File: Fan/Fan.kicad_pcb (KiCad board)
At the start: 2 copper layers, 32.5 x 14.5 mm, 25 parts, among them Q1 Hum Sensor, U2 HEF4093B

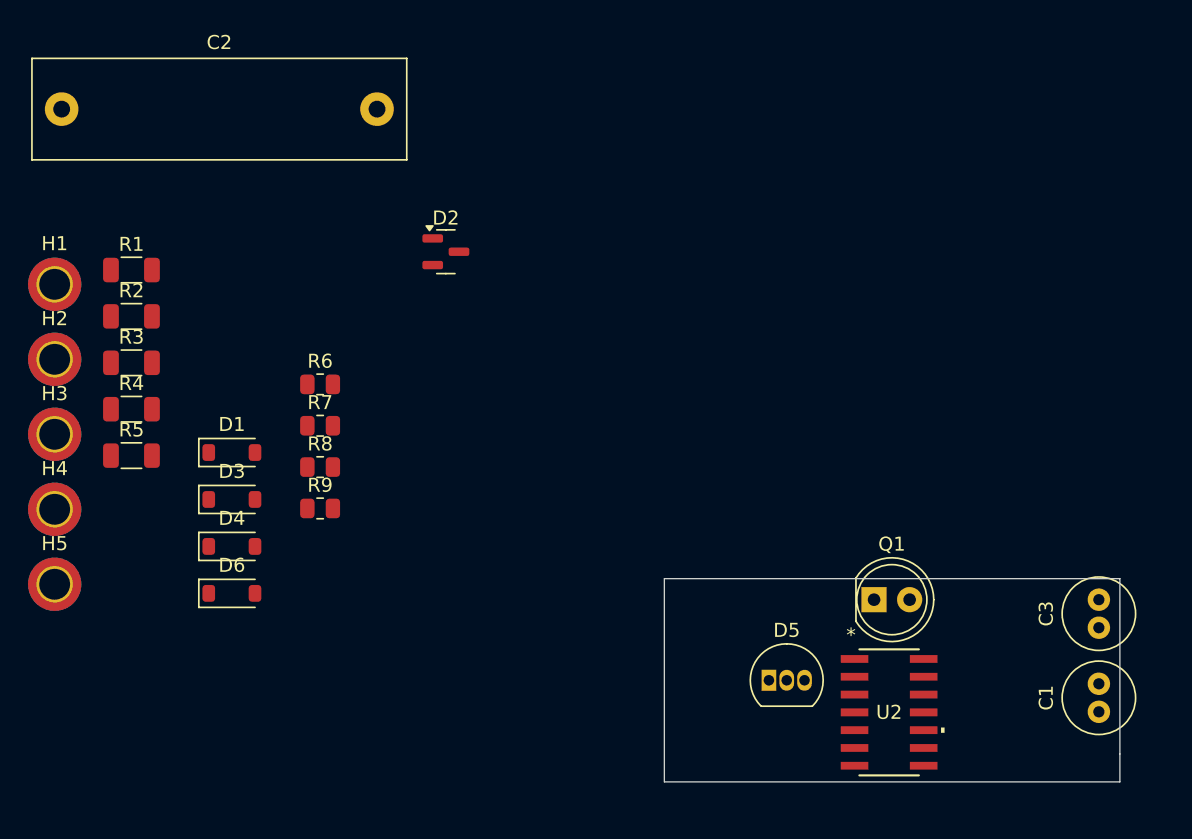
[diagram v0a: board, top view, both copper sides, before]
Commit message: update schematic, start working on PCB
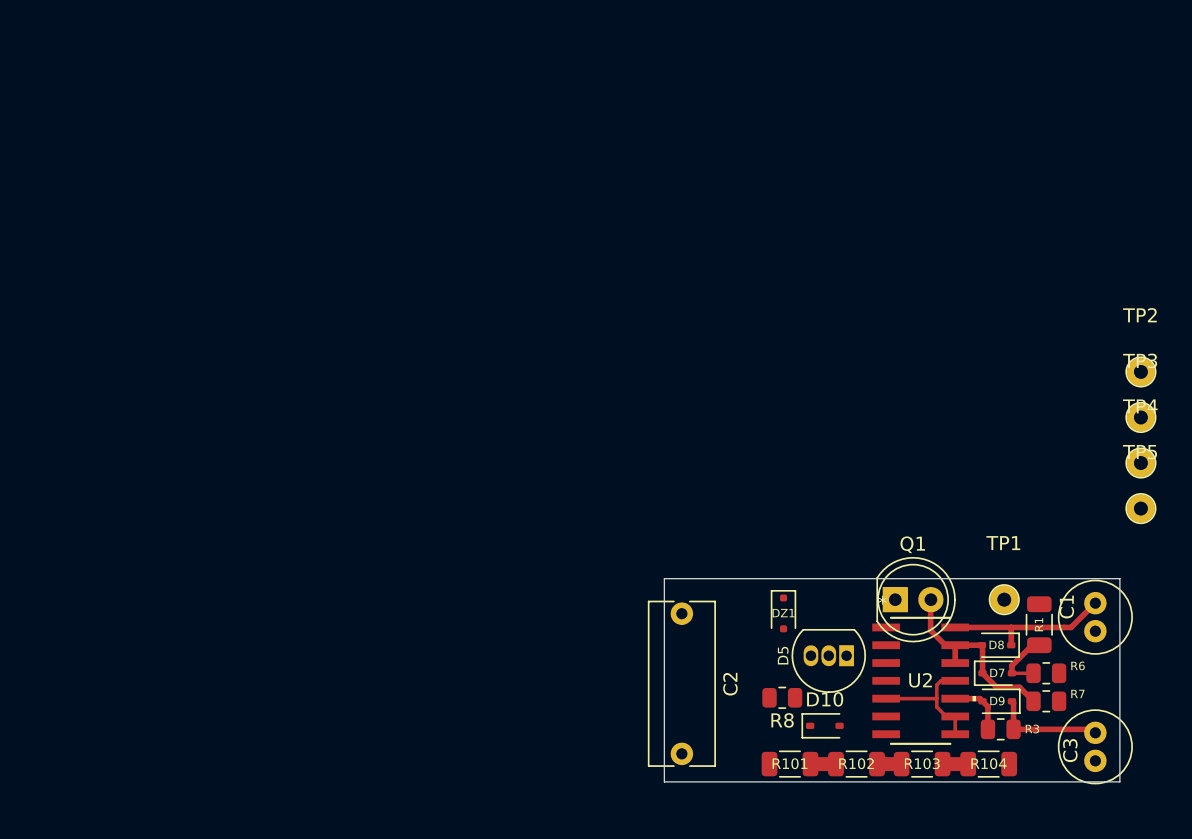
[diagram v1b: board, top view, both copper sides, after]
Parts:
- removed D1, D3, D4, D6: 1N4148W, Diode_SMD:D_SOD-123
- removed D2: BZX84Cxx, Package_TO_SOT_SMD:SOT-23
- removed H1, H2, H3, H4, H5: MountingHole_Pad, MountingHole:MountingHole_2.2mm_M2_DIN965_Pad_TopBottom
- added D10: 1N4148WS, Diode_SMD:D_SOD-323, F.Cu at (112.0, 62.5)
- added D7: 1N4148WS, Diode_SMD:D_SOD-323, F.Cu at (124.2, 58.8)
- added D8: 1N4148WS, Diode_SMD:D_SOD-323, F.Cu at (124.2, 56.8)
- added D9: 1N4148WS, Diode_SMD:D_SOD-323, F.Cu at (124.2, 60.8)
- added DZ1: BZX84J-C12,115, Diode_SMD:D_SOD-323F, F.Cu at (109.0, 54.5)
- added TP1: TestPoint, Pads:TestPoint_Top_Hole_D2.0mm, F.Cu at (124.8, 53.5)
- added TP2: TestPoint, Pads:TestPoint_Top_Hole_D2.0mm, F.Cu at (134.5, 37.2)
- added TP3: TestPoint, Pads:TestPoint_Top_Hole_D2.0mm, F.Cu at (134.5, 40.5)
- added TP4: TestPoint, Pads:TestPoint_Top_Hole_D2.0mm, F.Cu at (134.5, 43.8)
- added TP5: TestPoint, Pads:TestPoint_Top_Hole_D2.0mm, F.Cu at (134.5, 47.0)
- C2: footprint Capacitor_THT:C_Rect_L26.5mm_W7.0mm_P22.50mm_MKS4 -> Capacitor_THT:C_Rect_L11.5mm_W4.5mm_P10.00mm_MKT
- moved R104 66.2 mm to (123.6, 65.2), turned to 180 degrees
- moved R1 65.9 mm to (127.2, 55.3), turned to -90 degrees
- moved R103 63.3 mm to (118.9, 65.2), turned to 180 degrees
- moved R102 60.8 mm to (114.2, 65.2), turned to 180 degrees
- moved R101 58.7 mm to (109.5, 65.2), turned to 180 degrees
- moved C2 57.0 mm to (101.8, 54.5), turned to -90 degrees
- moved R7 56.5 mm to (127.8, 60.8)
- moved R6 54.7 mm to (127.8, 58.8)
- moved R3 51.1 mm to (124.5, 62.8)
- moved R8 36.9 mm to (108.9, 60.5), turned to 180 degrees
- moved C1 7.75 mm to (131.2, 53.8), turned to -90 degrees
- moved C3 7.50 mm to (131.2, 63.0), turned to -90 degrees
- moved D5 5.81 mm to (113.5, 57.5), turned to 180 degrees
- moved U2 3.18 mm to (118.8, 59.3)
- moved Q1 1.52 mm to (117.0, 53.5)
- renumbered R5 to R1, R1 to R101, R2 to R102, R3 to R103, R4 to R104, R9 to R3, R7 to R6, R6 to R7
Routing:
- net Net-(D7-K): track 0.00 -> 14.3 mm
- net +12V: track 0.00 -> 12.0 mm
- net Net-(U2-Pad11): track 0.00 -> 9.51 mm
- net Net-(D9-K): track 0.00 -> 7.99 mm
- net Net-(D7-A): track 0.00 -> 4.64 mm
- net Net-(D9-A): track 0.00 -> 4.19 mm
- net Net-(R103-Pad1): track 0.00 -> 1.83 mm
- net Net-(R101-Pad1): track 0.00 -> 1.83 mm
- net Net-(R102-Pad1): track 0.00 -> 1.75 mm
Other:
- outline, holes or cut-outs redrawn

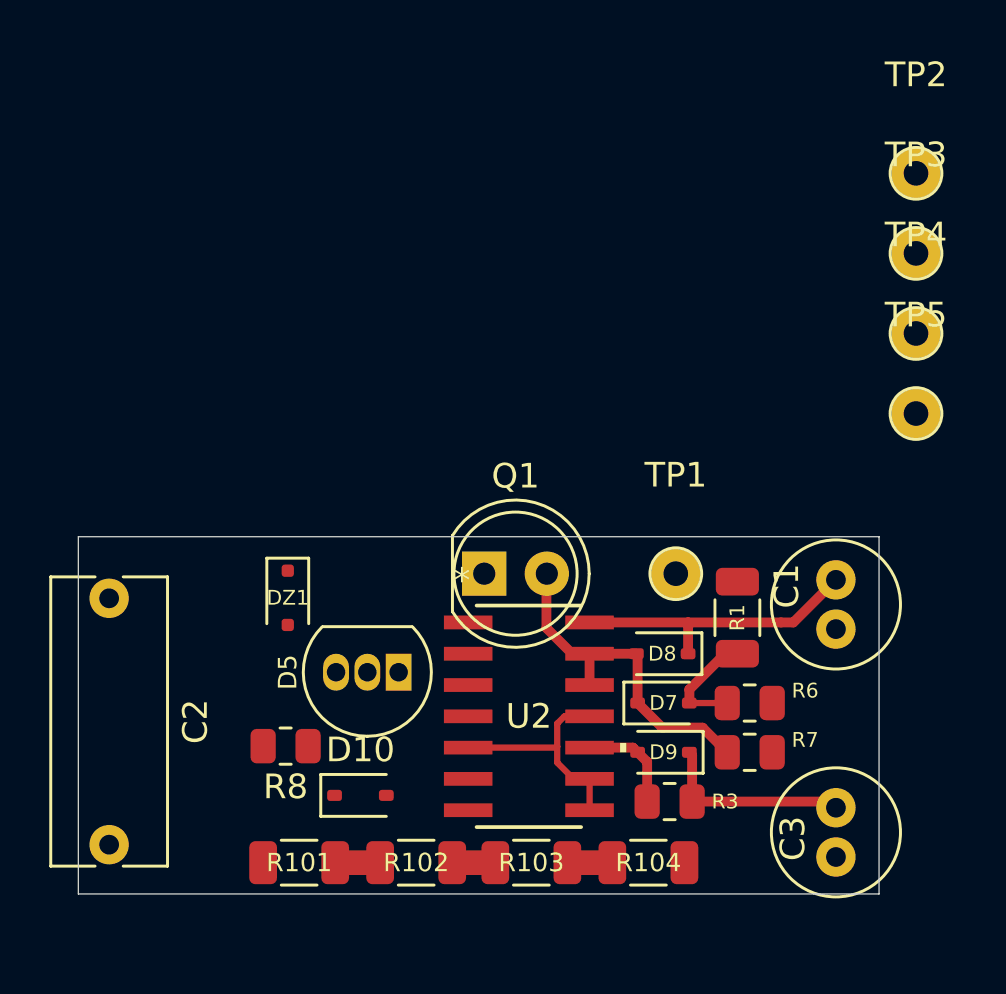
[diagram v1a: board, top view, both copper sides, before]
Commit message: pcb and schematic for feedback
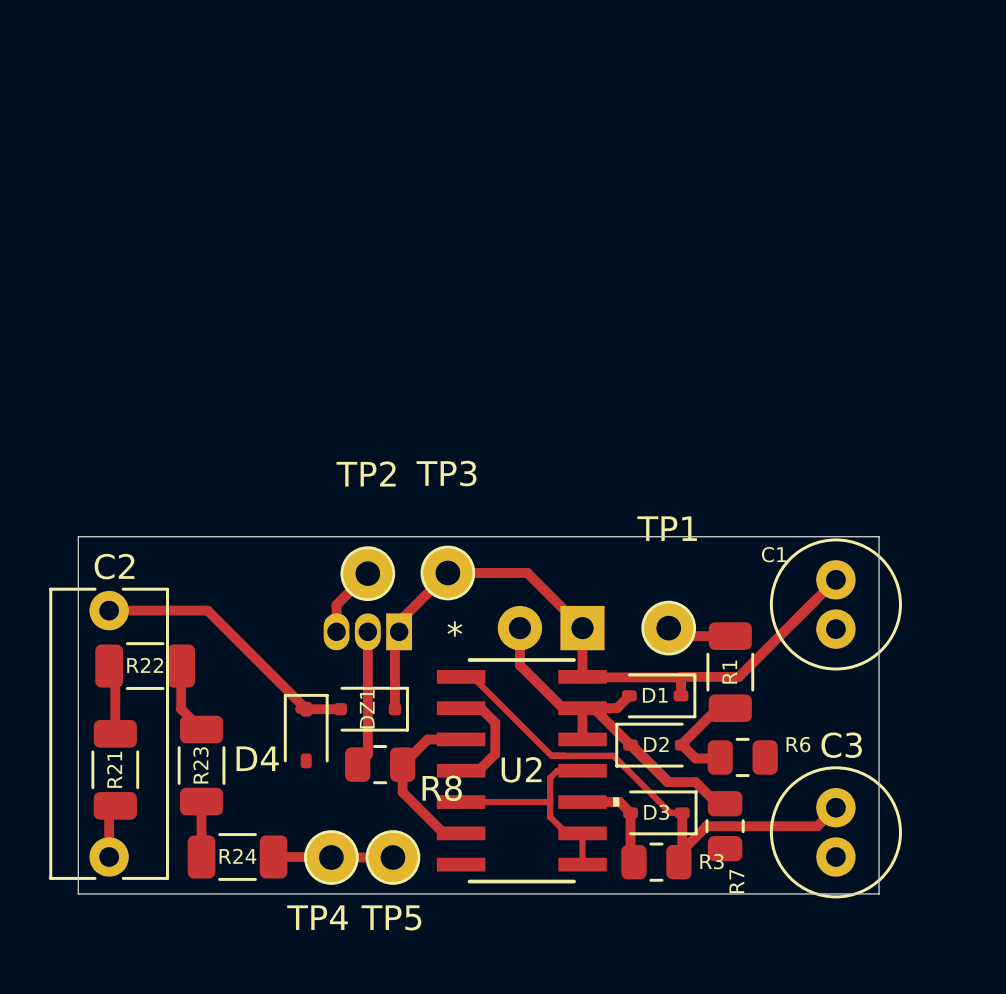
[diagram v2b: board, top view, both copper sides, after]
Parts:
- D5, Q1: moved to B.Cu
- moved TP4 31.9 mm to (110.8, 65.0)
- moved TP5 27.8 mm to (113.3, 65.0)
- moved TP2 27.6 mm to (112.2, 53.5)
- moved TP3 23.0 mm to (115.5, 53.5)
- moved R24 16.7 mm to (107.0, 65.0)
- moved R23 14.0 mm to (105.5, 61.3), turned to 90 degrees
- moved R22 13.6 mm to (103.2, 57.2)
- moved R21 8.36 mm to (102.0, 61.5), turned to -90 degrees
- moved DZ1 5.57 mm to (112.2, 59.0), turned to 180 degrees
- moved Q1 4.56 mm to (121.0, 55.7), turned to 180 degrees
- moved R8 3.91 mm to (112.8, 61.2)
- moved D4 3.29 mm to (109.8, 60.0), turned to -90 degrees
- moved R7 3.16 mm to (126.8, 63.8), turned to -90 degrees
- moved R3 2.52 mm to (124.0, 65.2)
- moved D3 2.48 mm to (124.0, 63.2)
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- renumbered D8 to D1, D7 to D2, D9 to D3, D10 to D4, R101 to R21, R102 to R22, R103 to R23, R104 to R24
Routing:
- net +12V: track 12.0 -> 28.7 mm
- net Net-(D3-K): track 7.99 -> 23.1 mm
- net Net-(D4-K): track 0.00 -> 11.3 mm
- net Net-(R8-Pad1): track 0.00 -> 6.98 mm
- net Net-(D5-G): track 0.00 -> 6.27 mm
- net Net-(R24-Pad1): track 0.00 -> 4.85 mm
- net Net-(U2-Pad2): track 0.00 -> 4.57 mm
- net Net-(D1-A): track 14.3 -> 17.6 mm
- net Net-(D5-A2): track 0.00 -> 2.89 mm
- net Net-(R1-Pad1): track 0.00 -> 2.63 mm
- net Net-(C2-Pad2): track 0.00 -> 2.18 mm
- net Net-(R22-Pad1): track 1.75 -> 2.92 mm
- net Net-(R21-Pad1): track 1.83 -> 2.85 mm
